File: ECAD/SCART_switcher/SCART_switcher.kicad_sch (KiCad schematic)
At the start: 0 parts

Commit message: progressed ecad
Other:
- sheet SCART input 10 ports: added none; removed 4_3_FORMAT
- sheet SCART input 2 ports: added none; removed 4_3_FORMAT
- sheet SCART input 3 ports: added none; removed 4_3_FORMAT
- sheet SCART input 4 ports: added none; removed 4_3_FORMAT
- sheet SCART input 5 ports: added none; removed 4_3_FORMAT
- sheet SCART input 6 ports: added none; removed 4_3_FORMAT
- sheet SCART input 7 ports: added none; removed 4_3_FORMAT
- sheet SCART input 8 ports: added none; removed 4_3_FORMAT
- sheet SCART input 9 ports: added none; removed 4_3_FORMAT
- sheet SCART output ports: added none; removed 4_3_FORMAT

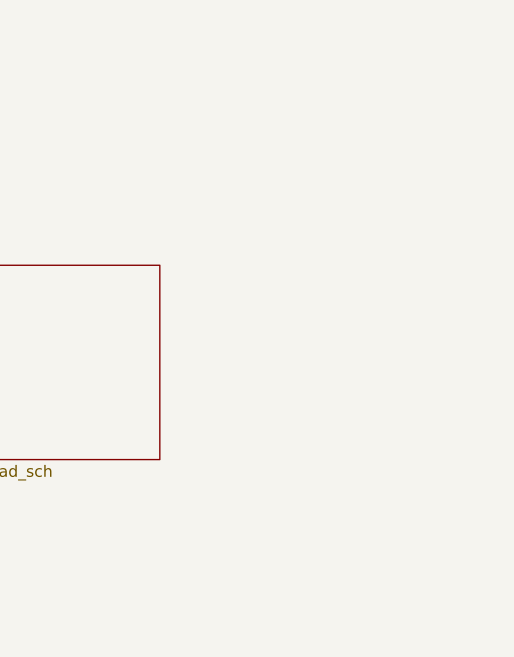
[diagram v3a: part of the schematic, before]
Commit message: Update SCART_switcher.kicad_sch
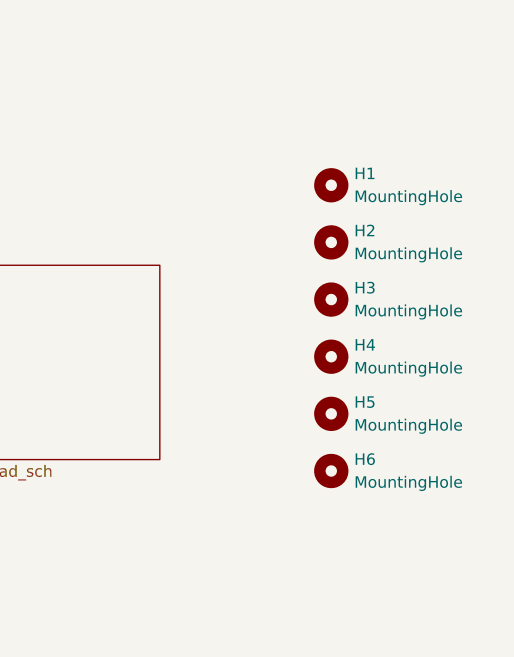
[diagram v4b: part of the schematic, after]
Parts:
- added H1, H2, H3, H4, H5, H6: MountingHole, MountingHole:MountingHole_3.2mm_M3, symbol Mechanical:MountingHole
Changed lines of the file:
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@@
     (effects (font (size 1.27 1.27)) (justify right bottom))
+  )
+  (symbol (lib_id "Mechanical:MountingHole") (at 260.35 132.08 0) (unit 1)
+    (in_bom yes) (on_board yes) (dnp no) (fields_autoplaced)
+    (property "Reference" "H2" (at 262.89 130.81 0)
+      (effects (font (size 1.27 1.27)) (justify left))
+    )
+    (property "Value" "MountingHole" (at 262.89 133.35 0)
+      (effects (font (size 1.27 1.27)) (justify left))
+    )
+    (property "Footprint" "MountingHole:MountingHole_3.2mm_M3" (at 260.35 132.08 0)
+      (effects (font (size 1.27 1.27)) hide)
+    )
+    (property "Datasheet" "~" (at 260.35 132.08 0)
+      (effects (font (size 1.27 1.27)) hide)
+    )
+    (instances
+      (project "SCART_switcher"
+        (path "/8cd08eb5-4755-4ef5-8eeb-77fd9974b180"
+          (reference "H2") (unit 1)
+        )
+      )
+    )
+  )
+  (symbol (lib_id "Mechanical:MountingHole") (at 260.35 125.73 0) (unit 1)
+    (in_bom yes) (on_board yes) (dnp no) (fields_autoplaced)
+    (property "Reference" "H1" (at 262.89 124.46 0)
+      (effects (font (size 1.27 1.27)) (justify left))
+    )
+    (property "Value" "MountingHole" (at 262.89 127 0)
+      (effects (font (size 1.27 1.27)) (justify left))
+    )
+    (property "Footprint" "MountingHole:MountingHole_3.2mm_M3" (at 260.35 125.73 0)
+      (effects (font (size 1.27 1.27)) hide)
+    )
+    (property "Datasheet" "~" (at 260.35 125.73 0)
+      (effects (font (size 1.27 1.27)) hide)
+    )
+    (instances
+      (project "SCART_switcher"
+        (path "/8cd08eb5-4755-4ef5-8eeb-77fd9974b180"
+          (reference "H1") (unit 1)
+        )
+      )
+    )
+  )
+  (symbol (lib_id "Mechanical:MountingHole") (at 260.35 151.13 0) (unit 1)
+    (in_bom yes) (on_board yes) (dnp no) (fields_autoplaced)
+    (property "Reference" "H5" (at 262.89 149.86 0)
+      (effects (font (size 1.27 1.27)) (justify left))
+    )
+    (property "Value" "MountingHole" (at 262.89 152.4 0)
+      (effects (font (size 1.27 1.27)) (justify left))
+    )
+    (property "Footprint" "MountingHole:MountingHole_3.2mm_M3" (at 260.35 151.13 0)
+      (effects (font (size 1.27 1.27)) hide)
+    )
+    (property "Datasheet" "~" (at 260.35 151.13 0)
+      (effects (font (size 1.27 1.27)) hide)
+    )
+    (instances
+      (project "SCART_switcher"
+        (path "/8cd08eb5-4755-4ef5-8eeb-77fd9974b180"
+          (reference "H5") (unit 1)
+        )
+      )
+    )
+  )
+  (symbol (lib_id "Mechanical:MountingHole") (at 260.35 157.48 0) (unit 1)
+    (in_bom yes) (on_board yes) (dnp no) (fields_autoplaced)
+    (property "Reference" "H6" (at 262.89 156.21 0)
+      (effects (font (size 1.27 1.27)) (justify left))
+    )
+    (property "Value" "MountingHole" (at 262.89 158.75 0)
+      (effects (font (size 1.27 1.27)) (justify left))
+    )
+    (property "Footprint" "MountingHole:MountingHole_3.2mm_M3" (at 260.35 157.48 0)
+      (effects (font (size 1.27 1.27)) hide)
+    )
+    (property "Datasheet" "~" (at 260.35 157.48 0)
+      (effects (font (size 1.27 1.27)) hide)
+    )
+    (instances
+      (project "SCART_switcher"
+        (path "/8cd08eb5-4755-4ef5-8eeb-77fd9974b180"
+          (reference "H6") (unit 1)
+        )
+      )
+    )
+  )
+  (symbol (lib_id "Mechanical:MountingHole") (at 260.35 144.78 0) (unit 1)
+    (in_bom yes) (on_board yes) (dnp no) (fields_autoplaced)
+    (property "Reference" "H4" (at 262.89 143.51 0)
+      (effects (font (size 1.27 1.27)) (justify left))
+    )
+    (property "Value" "MountingHole" (at 262.89 146.05 0)
+      (effects (font (size 1.27 1.27)) (justify left))
+    )
+    (property "Footprint" "MountingHole:MountingHole_3.2mm_M3" (at 260.35 144.78 0)
+      (effects (font (size 1.27 1.27)) hide)
+    )
+    (property "Datasheet" "~" (at 260.35 144.78 0)
+      (effects (font (size 1.27 1.27)) hide)
+    )
+    (instances
+      (project "SCART_switcher"
+        (path "/8cd08eb5-4755-4ef5-8eeb-77fd9974b180"
+          (reference "H4") (unit 1)
+        )
+      )
+    )
+  )
+  (symbol (lib_id "Mechanical:MountingHole") (at 260.35 138.43 0) (unit 1)
+    (in_bom yes) (on_board yes) (dnp no) (fields_autoplaced)
+    (property "Reference" "H3" (at 262.89 137.16 0)
+      (effects (font (size 1.27 1.27)) (justify left))
+    )
+    (property "Value" "MountingHole" (at 262.89 139.7 0)
+      (effects (font (size 1.27 1.27)) (justify left))
+    )
+    (property "Footprint" "MountingHole:MountingHole_3.2mm_M3" (at 260.35 138.43 0)
+      (effects (font (size 1.27 1.27)) hide)
+    )
+    (property "Datasheet" "~" (at 260.35 138.43 0)
+      (effects (font (size 1.27 1.27)) hide)
+    )
+    (instances
+      (project "SCART_switcher"
+        (path "/8cd08eb5-4755-4ef5-8eeb-77fd9974b180"
+          (reference "H3") (unit 1)
+        )
+      )
+    )
   )
   (sheet (at 111.76 81.28) (size 30.48 25.4) (fields_autoplaced)

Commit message: Progressed ECAD.
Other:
- added sheet Dummy input (dummy_input.kicad_sch)
- moved on the sheet: H1, H2, H3, H4, H5, H6

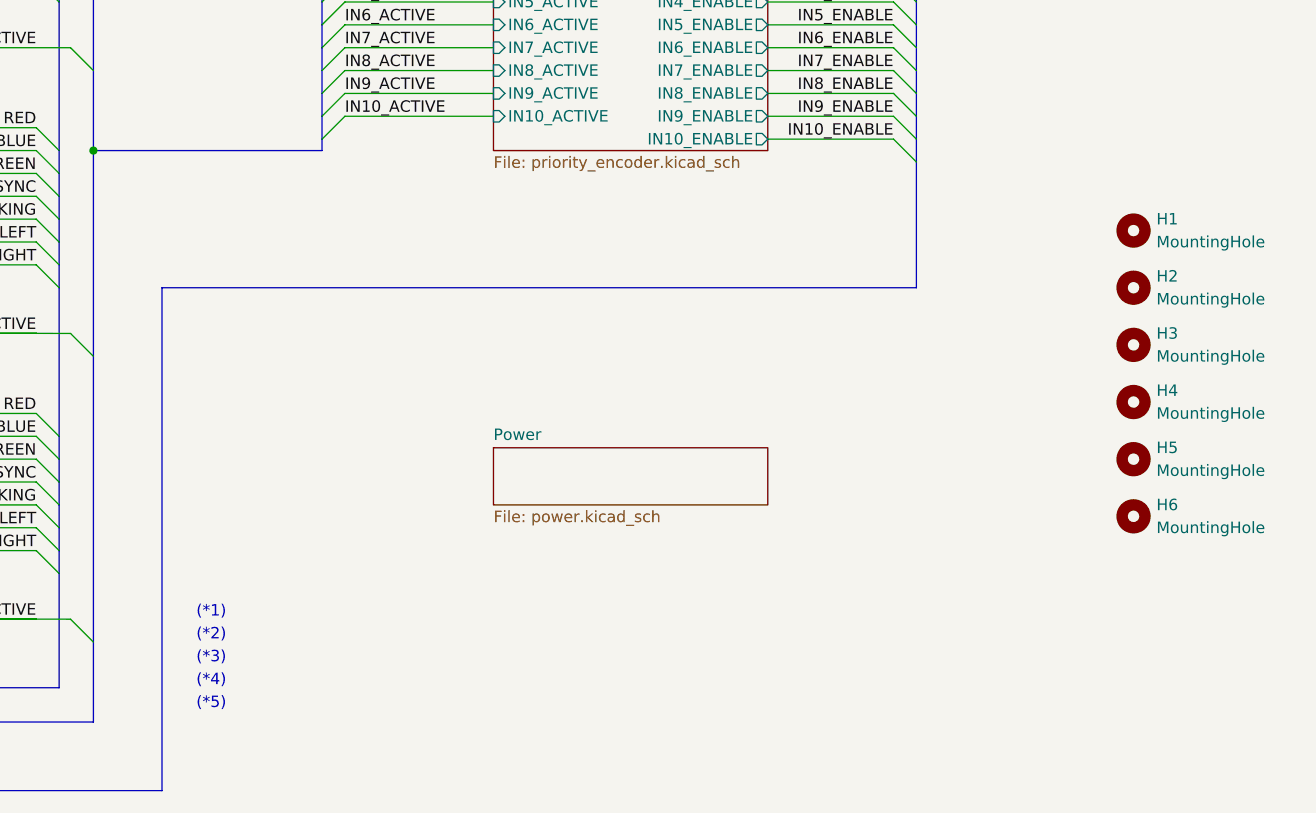
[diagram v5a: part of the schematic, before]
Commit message: Update SCART_switcher.kicad_sch
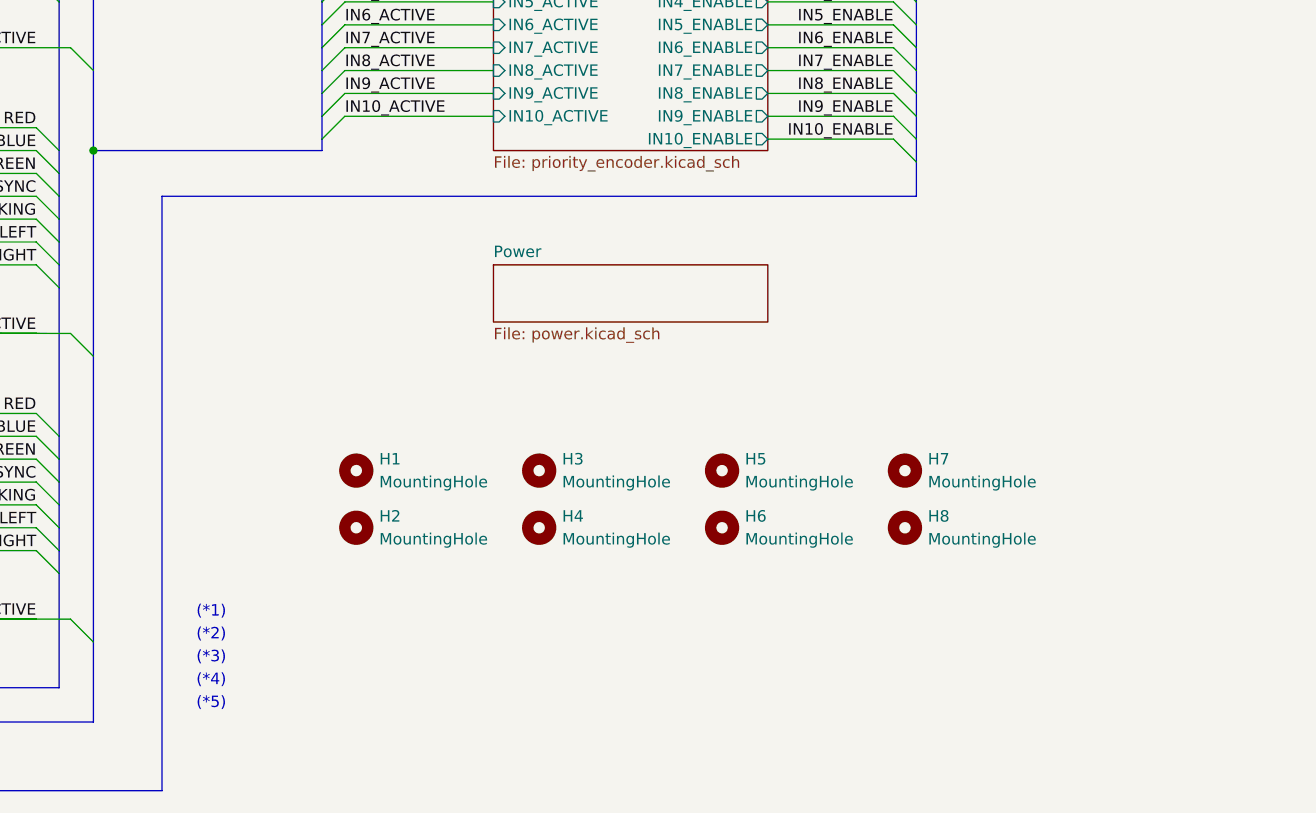
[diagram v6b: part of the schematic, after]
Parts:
- added H7, H8: MountingHole, MountingHole:MountingHole_3.2mm_M3, symbol Mechanical:MountingHole
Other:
- moved on the sheet: H1, H2, H3, H4, H5, H6
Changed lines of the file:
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@@
     (stroke (width 0) (type default))
   )
-  (bus (pts (xy 173.99 132.08) (xy 257.81 132.08))
+  (bus (pts (xy 173.99 121.92) (xy 257.81 121.92))
     (stroke (width 0) (type default))
   )
@@
     (stroke (width 0) (type default))
   )
-  (bus (pts (xy 257.81 118.11) (xy 257.81 132.08))
+  (bus (pts (xy 257.81 118.11) (xy 257.81 121.92))
     (stroke (width 0) (type default))
   )
@@
     (stroke (width 0) (type default))
   )
-  (bus (pts (xy 173.99 132.08) (xy 173.99 187.96))
+  (bus (pts (xy 173.99 121.92) (xy 173.99 187.96))
     (stroke (width 0) (type default))
   )
@@
     (effects (font (size 1.27 1.27)) (justify right bottom))
   )
-  (symbol (lib_id "Mechanical:MountingHole") (at 281.94 132.08 0) (unit 1)
+  (symbol (lib_id "Mechanical:MountingHole") (at 195.58 158.75 0) (unit 1)
     (in_bom yes) (on_board yes) (dnp no) (fields_autoplaced)
-    (property "Reference" "H2" (at 284.48 130.81 0)
-      (effects (font (size 1.27 1.27)) (justify left))
-    )
-    (property "Value" "MountingHole" (at 284.48 133.35 0)
-      (effects (font (size 1.27 1.27)) (justify left))
-    )
-    (property "Footprint" "MountingHole:MountingHole_3.2mm_M3" (at 281.94 132.08 0)
-      (effects (font (size 1.27 1.27)) hide)
-    )
-    (property "Datasheet" "~" (at 281.94 132.08 0)
+    (property "Reference" "H2" (at 198.12 157.48 0)
+      (effects (font (size 1.27 1.27)) (justify left))
+    )
+    (property "Value" "MountingHole" (at 198.12 160.02 0)
+      (effects (font (size 1.27 1.27)) (justify left))
+    )
+    (property "Footprint" "MountingHole:MountingHole_3.2mm_M3" (at 195.58 158.75 0)
+      (effects (font (size 1.27 1.27)) hide)
+    )
+    (property "Datasheet" "~" (at 195.58 158.75 0)
       (effects (font (size 1.27 1.27)) hide)
     )
@@
     )
   )
-  (symbol (lib_id "Mechanical:MountingHole") (at 281.94 125.73 0) (unit 1)
+  (symbol (lib_id "Mechanical:MountingHole") (at 195.58 152.4 0) (unit 1)
     (in_bom yes) (on_board yes) (dnp no) (fields_autoplaced)
-    (property "Reference" "H1" (at 284.48 124.46 0)
-      (effects (font (size 1.27 1.27)) (justify left))
-    )
-    (property "Value" "MountingHole" (at 284.48 127 0)
-      (effects (font (size 1.27 1.27)) (justify left))
-    )
-    (property "Footprint" "MountingHole:MountingHole_3.2mm_M3" (at 281.94 125.73 0)
-      (effects (font (size 1.27 1.27)) hide)
-    )
-    (property "Datasheet" "~" (at 281.94 125.73 0)
+    (property "Reference" "H1" (at 198.12 151.13 0)
+      (effects (font (size 1.27 1.27)) (justify left))
+    )
+    (property "Value" "MountingHole" (at 198.12 153.67 0)
+      (effects (font (size 1.27 1.27)) (justify left))
+    )
+    (property "Footprint" "MountingHole:MountingHole_3.2mm_M3" (at 195.58 152.4 0)
+      (effects (font (size 1.27 1.27)) hide)
+    )
+    (property "Datasheet" "~" (at 195.58 152.4 0)
       (effects (font (size 1.27 1.27)) hide)
     )
@@
     )
   )
-  (symbol (lib_id "Mechanical:MountingHole") (at 281.94 151.13 0) (unit 1)
+  (symbol (lib_id "Mechanical:MountingHole") (at 236.22 152.4 0) (unit 1)
     (in_bom yes) (on_board yes) (dnp no) (fields_autoplaced)
-    (property "Reference" "H5" (at 284.48 149.86 0)
-      (effects (font (size 1.27 1.27)) (justify left))
-    )
-    (property "Value" "MountingHole" (at 284.48 152.4 0)
-      (effects (font (size 1.27 1.27)) (justify left))
-    )
-    (property "Footprint" "MountingHole:MountingHole_3.2mm_M3" (at 281.94 151.13 0)
-      (effects (font (size 1.27 1.27)) hide)
-    )
-    (property "Datasheet" "~" (at 281.94 151.13 0)
+    (property "Reference" "H5" (at 238.76 151.13 0)
+      (effects (font (size 1.27 1.27)) (justify left))
+    )
+    (property "Value" "MountingHole" (at 238.76 153.67 0)
+      (effects (font (size 1.27 1.27)) (justify left))
+    )
+    (property "Footprint" "MountingHole:MountingHole_3.2mm_M3" (at 236.22 152.4 0)
+      (effects (font (size 1.27 1.27)) hide)
+    )
+    (property "Datasheet" "~" (at 236.22 152.4 0)
       (effects (font (size 1.27 1.27)) hide)
     )
@@
     )
   )
-  (symbol (lib_id "Mechanical:MountingHole") (at 281.94 157.48 0) (unit 1)
+  (symbol (lib_id "Mechanical:MountingHole") (at 236.22 158.75 0) (unit 1)
     (in_bom yes) (on_board yes) (dnp no) (fields_autoplaced)
-    (property "Reference" "H6" (at 284.48 156.21 0)
-      (effects (font (size 1.27 1.27)) (justify left))
-    )
-    (property "Value" "MountingHole" (at 284.48 158.75 0)
-      (effects (font (size 1.27 1.27)) (justify left))
-    )
-    (property "Footprint" "MountingHole:MountingHole_3.2mm_M3" (at 281.94 157.48 0)
-      (effects (font (size 1.27 1.27)) hide)
-    )
-    (property "Datasheet" "~" (at 281.94 157.48 0)
+    (property "Reference" "H6" (at 238.76 157.48 0)
+      (effects (font (size 1.27 1.27)) (justify left))
+    )
+    (property "Value" "MountingHole" (at 238.76 160.02 0)
+      (effects (font (size 1.27 1.27)) (justify left))
+    )
+    (property "Footprint" "MountingHole:MountingHole_3.2mm_M3" (at 236.22 158.75 0)
+      (effects (font (size 1.27 1.27)) hide)
+    )
+    (property "Datasheet" "~" (at 236.22 158.75 0)
       (effects (font (size 1.27 1.27)) hide)
     )
@@
     )
   )
-  (symbol (lib_id "Mechanical:MountingHole") (at 281.94 144.78 0) (unit 1)
+  (symbol (lib_id "Mechanical:MountingHole") (at 215.9 158.75 0) (unit 1)
     (in_bom yes) (on_board yes) (dnp no) (fields_autoplaced)
-    (property "Reference" "H4" (at 284.48 143.51 0)
-      (effects (font (size 1.27 1.27)) (justify left))
-    )
-    (property "Value" "MountingHole" (at 284.48 146.05 0)
-      (effects (font (size 1.27 1.27)) (justify left))
-    )
-    (property "Footprint" "MountingHole:MountingHole_3.2mm_M3" (at 281.94 144.78 0)
-      (effects (font (size 1.27 1.27)) hide)
-    )
-    (property "Datasheet" "~" (at 281.94 144.78 0)
+    (property "Reference" "H4" (at 218.44 157.48 0)
+      (effects (font (size 1.27 1.27)) (justify left))
+    )
+    (property "Value" "MountingHole" (at 218.44 160.02 0)
+      (effects (font (size 1.27 1.27)) (justify left))
+    )
+    (property "Footprint" "MountingHole:MountingHole_3.2mm_M3" (at 215.9 158.75 0)
+      (effects (font (size 1.27 1.27)) hide)
+    )
+    (property "Datasheet" "~" (at 215.9 158.75 0)
       (effects (font (size 1.27 1.27)) hide)
     )
@@
     )
   )
-  (symbol (lib_id "Mechanical:MountingHole") (at 281.94 138.43 0) (unit 1)
+  (symbol (lib_id "Mechanical:MountingHole") (at 256.54 152.4 0) (unit 1)
     (in_bom yes) (on_board yes) (dnp no) (fields_autoplaced)
-    (property "Reference" "H3" (at 284.48 137.16 0)
-      (effects (font (size 1.27 1.27)) (justify left))
-    )
-    (property "Value" "MountingHole" (at 284.48 139.7 0)
-      (effects (font (size 1.27 1.27)) (justify left))
-    )
-    (property "Footprint" "MountingHole:MountingHole_3.2mm_M3" (at 281.94 138.43 0)
-      (effects (font (size 1.27 1.27)) hide)
-    )
-    (property "Datasheet" "~" (at 281.94 138.43 0)
+    (property "Reference" "H7" (at 259.08 151.13 0)
+      (effects (font (size 1.27 1.27)) (justify left))
+    )
+    (property "Value" "MountingHole" (at 259.08 153.67 0)
+      (effects (font (size 1.27 1.27)) (justify left))
+    )
+    (property "Footprint" "MountingHole:MountingHole_3.2mm_M3" (at 256.54 152.4 0)
+      (effects (font (size 1.27 1.27)) hide)
+    )
+    (property "Datasheet" "~" (at 256.54 152.4 0)
+      (effects (font (size 1.27 1.27)) hide)
+    )
+    (instances
+      (project "SCART_switcher"
+        (path "/8cd08eb5-4755-4ef5-8eeb-77fd9974b180"
+          (reference "H7") (unit 1)
+        )
+      )
+    )
+  )
+  (symbol (lib_id "Mechanical:MountingHole") (at 256.54 158.75 0) (unit 1)
+    (in_bom yes) (on_board yes) (dnp no) (fields_autoplaced)
+    (property "Reference" "H8" (at 259.08 157.48 0)
+      (effects (font (size 1.27 1.27)) (justify left))
+    )
+    (property "Value" "MountingHole" (at 259.08 160.02 0)
+      (effects (font (size 1.27 1.27)) (justify left))
+    )
+    (property "Footprint" "MountingHole:MountingHole_3.2mm_M3" (at 256.54 158.75 0)
+      (effects (font (size 1.27 1.27)) hide)
+    )
+    (property "Datasheet" "~" (at 256.54 158.75 0)
+      (effects (font (size 1.27 1.27)) hide)
+    )
+    (instances
+      (project "SCART_switcher"
+        (path "/8cd08eb5-4755-4ef5-8eeb-77fd9974b180"
+          (reference "H8") (unit 1)
+        )
+      )
+    )
+  )
+  (symbol (lib_id "Mechanical:MountingHole") (at 215.9 152.4 0) (unit 1)
+    (in_bom yes) (on_board yes) (dnp no) (fields_autoplaced)
+    (property "Reference" "H3" (at 218.44 151.13 0)
+      (effects (font (size 1.27 1.27)) (justify left))
+    )
+    (property "Value" "MountingHole" (at 218.44 153.67 0)
+      (effects (font (size 1.27 1.27)) (justify left))
+    )
+    (property "Footprint" "MountingHole:MountingHole_3.2mm_M3" (at 215.9 152.4 0)
+      (effects (font (size 1.27 1.27)) hide)
+    )
+    (property "Datasheet" "~" (at 215.9 152.4 0)
       (effects (font (size 1.27 1.27)) hide)
     )
@@
     )
   )
-  (sheet (at 210.82 149.86) (size 30.48 6.35) (fields_autoplaced)
+  (sheet (at 210.82 129.54) (size 30.48 6.35) (fields_autoplaced)
     (stroke (width 0.1524) (type solid))
     (fill (color 0 0 0 0.0000))
-    (property "Sheetname" "Power" (at 210.82 149.1484 0)
+    (property "Sheetname" "Power" (at 210.82 128.8284 0)
       (effects (font (size 1.27 1.27)) (justify left bottom))
     )
-    (property "Sheetfile" "power.kicad_sch" (at 210.82 156.7946 0)
+    (property "Sheetfile" "power.kicad_sch" (at 210.82 136.4746 0)
       (effects (font (size 1.27 1.27)) (justify left top))
     )
